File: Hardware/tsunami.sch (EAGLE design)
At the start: 154 parts, among them J1 CORTEX_DEBUGPTH, J10 3.3V, J100 AUDIO I/O, J101 USD-SDIO-SOCKET, J102 USB-MICROB", J12 !PLAYING, J3 FTDI_DEVICE, J5 AOUT5L, J6 AOUT5R, J7 AIN2L, J8 AIN2R, J9 3.3VA, Q1 2.5A/30V, U1 ATSAMS70NXXA-AN, U2 AK4618VQSFE-PACKAGE, U3 LM1117, U4 LM1117, U5 6N138M, U6 74AHC1G125, Y2 11.2896 MHz

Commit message: Somehow forgot schem with last commit.
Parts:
- removed J100: AUDIO I/O, SparkFun-Connectors:M10X2
- removed J101: USD-SDIO-SOCKET, SparkFun-Connectors:USD-SDIO-SOCKET
- removed J102: USB-MICROB", SparkFun-Connectors:USB-MICROB"
- removed J16, J17: (no value), SparkFun-Connectors:M02PTH
- added J13: GND, SparkFun-Connectors:M01PTH_NO_SILK_YES_STOP
- added TP1: AIN2L, SparkFun-Passives:TEST-POINTTP_15TH_THRU
- added TP2: AIN2R, SparkFun-Passives:TEST-POINTTP_15TH_THRU
- added TP3: AOUT5L, SparkFun-Passives:TEST-POINTTP_15TH_THRU
- added TP4: AOUT5R, SparkFun-Passives:TEST-POINTTP_15TH_THRU
- C1: value 12pF -> 10nF; device SparkFun-Capacitors:12PF-50V-5%(0603) -> SparkFun-Capacitors:10NF/10000PF-50V-10%(0603)
- C12: value 10uF -> 0.1uF; device SparkFun-Capacitors:10UF-6.3V-20%(0603) -> SparkFun-Capacitors:0.1UF-25V(+80/-20%)(0603)
- C13, C15, C17, C19, C21, C22, C23, C24, C26, C28, C31: value 1.0uF -> 0.1uF; device SparkFun-Capacitors:1.0UF-16V-10%(0603) -> SparkFun-Capacitors:0.1UF-25V(+80/-20%)(0603)
- C14: value 0.1uF -> 4.7uF; device SparkFun-Capacitors:0.1UF-25V(+80/-20%)(0603) -> SparkFun-Capacitors:4.7UF-6.3V-10%(0603)0603
- C2: value 12pF -> 10uF; device SparkFun-Capacitors:12PF-50V-5%(0603) -> SparkFun-Capacitors:10UF-6.3V-20%(0603)
- C20: value 1.0uF -> 10pF; device SparkFun-Capacitors:1.0UF-16V-10%(0603) -> SparkFun-Capacitors:10PF-50V-5%(0603)
- C25: value 1.0uF -> 2.2uF; device SparkFun-Capacitors:1.0UF-16V-10%(0603) -> SparkFun-Capacitors:2.2UF-10V-20%(0603)
- C27: value 1.0uF -> 10uF; device SparkFun-Capacitors:1.0UF-16V-10%(0603) -> SparkFun-Capacitors:10UF-6.3V-20%(0603)
- C29: value 4.7uF -> 1.0uF; device SparkFun-Capacitors:4.7UF-6.3V-10%(0603)0603 -> SparkFun-Capacitors:1.0UF-16V-10%(0603)
- C30: value 10nF -> 1.0uF; device SparkFun-Capacitors:10NF/10000PF-50V-10%(0603) -> SparkFun-Capacitors:1.0UF-16V-10%(0603)
- C33, C39, C40, C41, C42, C43, C44, C45, C46: value 0.1uF -> 1.0uF; device SparkFun-Capacitors:0.1UF-25V(+80/-20%)(0603) -> SparkFun-Capacitors:1.0UF-16V-10%(0603)
- C34: value 10pF -> 1.0uF; device SparkFun-Capacitors:10PF-50V-5%(0603) -> SparkFun-Capacitors:1.0UF-16V-10%(0603)
- C36: value 10uF -> 1.0uF; device SparkFun-Capacitors:10UF-6.3V-20%(0603) -> SparkFun-Capacitors:1.0UF-16V-10%(0603)
- C37: device SparkFun-Capacitors:0.1UF-25V-5%(0603) -> SparkFun-Capacitors:0.1UF-25V(+80/-20%)(0603)
- C38: value 0.1uF -> 1.0uF; device SparkFun-Capacitors:0.1UF-25V-5%(0603) -> SparkFun-Capacitors:1.0UF-16V-10%(0603)
- C47, C48: device SparkFun-Capacitors:0.1UF-25V(+80/-20%)(0603) -> SparkFun-Capacitors:0.1UF-25V-5%(0603)
- C5: value 0.1uF -> 10uF; device SparkFun-Capacitors:0.1UF-25V(+80/-20%)(0603) -> SparkFun-Capacitors:10UF-6.3V-20%(0603)
- C6: value 2.2uF -> 10uF; device SparkFun-Capacitors:2.2UF-10V-20%(0603) -> SparkFun-Capacitors:10UF-6.3V-20%(0603)
- C7, C9: value 10uF -> 12pF; device SparkFun-Capacitors:10UF-6.3V-20%(0603) -> SparkFun-Capacitors:12PF-50V-5%(0603)
- D1: value BLUE -> MBRA140; device SparkFun-LED:LED-BLUE0603 -> SparkFun-DiscreteSemi:DIODE-SCHOTTKY-MBRA140
- D2: value MBRA140 -> BLUE; device SparkFun-DiscreteSemi:DIODE-SCHOTTKY-MBRA140 -> SparkFun-LED:LED-BLUE0603
- J1: value CORTEX_DEBUGPTH -> VDC-IN; device SparkFun-Connectors:CORTEX_DEBUGPTH -> SparkFun-Connectors:M02PTH
- J10: value 3.3V -> TRIG2; device SparkFun-Connectors:M01PTH_NO_SILK_YES_STOP -> SparkFun-Connectors:M08X2
- J11: value (none) -> TRIG1; device SparkFun-Connectors:M05NO_SILK -> SparkFun-Connectors:M08X2
- J12: value !PLAYING -> USD-SDIO-SOCKET; device SparkFun-Connectors:M01PTH_NO_SILK_YES_STOP -> SparkFun-Connectors:USD-SDIO-SOCKET
- J14: value (none) -> AUDIO I/O; device SparkFun-Connectors:M08X2 -> SparkFun-Connectors:M10X2
- J15: value (none) -> MIDI; device SparkFun-Connectors:M01PTH_NO_SILK_YES_STOP -> SparkFun-Connectors:M05NO_SILK
- J2: value (none) -> GND-IN; device SparkFun-Connectors:M01PTH_NO_SILK_YES_STOP -> SparkFun-Connectors:M02PTH
- J3: value FTDI_DEVICE -> DEBUG; device SparkFun-Connectors:FTDI_DEVICE -> SparkFun-Connectors:M01PTH_NO_SILK_YES_STOP
- J4: value (none) -> USB-MICROB"; device SparkFun-Connectors:M08X2 -> SparkFun-Connectors:USB-MICROB"
- J5: value AOUT5L -> CORTEX_DEBUGPTH; device SparkFun-Passives:TEST-POINTTP_15TH_THRU -> SparkFun-Connectors:CORTEX_DEBUGPTH
- J6: value AOUT5R -> 3.3VA; device SparkFun-Passives:TEST-POINTTP_15TH_THRU -> SparkFun-Connectors:M01PTH_NO_SILK_YES_STOP
- J7: value AIN2L -> 3.3V; device SparkFun-Passives:TEST-POINTTP_15TH_THRU -> SparkFun-Connectors:M01PTH_NO_SILK_YES_STOP
- J8: value AIN2R -> !PLAYING; device SparkFun-Passives:TEST-POINTTP_15TH_THRU -> SparkFun-Connectors:M01PTH_NO_SILK_YES_STOP
- J9: value 3.3VA -> FTDI_DEVICE; device SparkFun-Connectors:M01PTH_NO_SILK_YES_STOP -> SparkFun-Connectors:FTDI_DEVICE
- L1: value 470 -> 10uH; device SparkFun-Passives:INDUCTOR0603 -> SparkFun-Passives:INDUCTOR0805; PROD_ID NDUC-12579 -> NDUC-13231
- L4: value 10uH -> 470; device SparkFun-Passives:INDUCTOR0805 -> SparkFun-Passives:INDUCTOR0603; PROD_ID NDUC-13231 -> NDUC-12579
- LOGO1: value SFE_LOGO_NAME_FLAME.2_INCH -> SFE_LOGO_NAME.2_INCH; device SparkFun-Aesthetics:SFE_LOGO_NAME_FLAME.2_INCH -> SparkFun-Aesthetics:SFE_LOGO_NAME.2_INCH
- LOGO3: value SFE_LOGO_NAME.2_INCH -> OSHW-LOGOM; device SparkFun-Aesthetics:SFE_LOGO_NAME.2_INCH -> SparkFun-Aesthetics:OSHW-LOGOM
- R1: value 100k -> 33; device SparkFun-Resistors:100KOHM-1/10W-1%(0603) -> SparkFun-Resistors:33OHM1/10W1%(0603)
- R11, R12: value 100k -> 240; device SparkFun-Resistors:100KOHM-1/10W-1%(0603) -> SparkFun-Resistors:240OHM1/10W1%(0603)
- R13: value 100k -> 330; device SparkFun-Resistors:100KOHM-1/10W-1%(0603) -> SparkFun-Resistors:330OHM1/10W1%(0603)
- R14: value 5.62k -> 4.7K; device SparkFun-Resistors:5.62KOHM1/10W1%(0603) -> SparkFun-Resistors:4.7KOHM-1/10W-1%(0603)
- R15: value 15K -> 4.7K; device SparkFun-Resistors:15KOHM1/10W1%(0603)0603 -> SparkFun-Resistors:4.7KOHM-1/10W-1%(0603)
- R16: value 22K -> 2.2; device SparkFun-Resistors:22KOHM1/10W1%(0603) -> SparkFun-Resistors:2.2OHM-1/10W-5%(0603)
- R17: value 2.2 -> 5.62k; device SparkFun-Resistors:2.2OHM-1/10W-5%(0603) -> SparkFun-Resistors:5.62KOHM1/10W1%(0603)
- R18: value 240 -> 10K; device SparkFun-Resistors:240OHM1/10W1%(0603) -> SparkFun-Resistors:10KOHM-1/10W-1%(0603)0603
- R19: value 240 -> 100k; device SparkFun-Resistors:240OHM1/10W1%(0603) -> SparkFun-Resistors:100KOHM-1/10W-1%(0603)
- R2: value 100k -> 1M; device SparkFun-Resistors:100KOHM-1/10W-1%(0603) -> SparkFun-Resistors:1MOHM-1/10W-1%(0603)
- R20, R21: value 390 -> 100k; device SparkFun-Resistors:390OHM1/10W1%(0603) -> SparkFun-Resistors:100KOHM-1/10W-1%(0603)
- R23, R3: value 100k -> 10K; device SparkFun-Resistors:100KOHM-1/10W-1%(0603) -> SparkFun-Resistors:10KOHM-1/10W-1%(0603)0603
- R24: value 100k -> 100; device SparkFun-Resistors:100KOHM-1/10W-1%(0603) -> SparkFun-Resistors:100OHM-1/10W-1%(0603)
- R25, R26: value 4.7K -> 100; device SparkFun-Resistors:4.7KOHM-1/10W-1%(0603) -> SparkFun-Resistors:100OHM-1/10W-1%(0603)
- R27: value 33 -> 100; device SparkFun-Resistors:33OHM1/10W1%(0603) -> SparkFun-Resistors:100OHM-1/10W-1%(0603)
- R28: value 10K -> 100; device SparkFun-Resistors:10KOHM-1/10W-1%(0603)0603 -> SparkFun-Resistors:100OHM-1/10W-1%(0603)
- R29: value 1M -> 100k; device SparkFun-Resistors:1MOHM-1/10W-1%(0603) -> SparkFun-Resistors:100KOHM-1/10W-1%(0603)
- R32, R33, R34, R35, R36: value 10 -> 100k; device SparkFun-Resistors:10OHM-1/10W-1%(0603)SMD -> SparkFun-Resistors:100KOHM-1/10W-1%(0603)
- R4: value 100k -> 15K; device SparkFun-Resistors:100KOHM-1/10W-1%(0603) -> SparkFun-Resistors:15KOHM1/10W1%(0603)0603
- R40, R41, R43, R44: value 100 -> 10; device SparkFun-Resistors:100OHM-1/10W-1%(0603) -> SparkFun-Resistors:10OHM-1/10W-1%(0603)SMD
- R42: value 220 -> 10; device SparkFun-Resistors:220OHM-1/10W-1%(0603) -> SparkFun-Resistors:10OHM-1/10W-1%(0603)SMD
- R45: value 100 -> 220; device SparkFun-Resistors:100OHM-1/10W-1%(0603) -> SparkFun-Resistors:220OHM-1/10W-1%(0603)
- R5: value 10K -> 22K; device SparkFun-Resistors:10KOHM-1/10W-1%(0603)0603 -> SparkFun-Resistors:22KOHM1/10W1%(0603)
- R6: value 10K -> 100k; device SparkFun-Resistors:10KOHM-1/10W-1%(0603)0603 -> SparkFun-Resistors:100KOHM-1/10W-1%(0603)
- R7: value 330 -> 390; device SparkFun-Resistors:330OHM1/10W1%(0603) -> SparkFun-Resistors:390OHM1/10W1%(0603)
- R8: value 100k -> 390; device SparkFun-Resistors:100KOHM-1/10W-1%(0603) -> SparkFun-Resistors:390OHM1/10W1%(0603)
- S3: value DNS -> User; device SparkFun-Electromechanical:SWITCH-MOMENTARY-2SIDE_EZ -> SparkFun-Electromechanical:SWITCH-MOMENTARY-2SMD
- S4: value User -> DNS; device SparkFun-Electromechanical:SWITCH-MOMENTARY-2SMD -> SparkFun-Electromechanical:SWITCH-MOMENTARY-2SIDE_EZ
- U1: value ATSAMS70NXXA-AN -> LM1117; device tapestry:ATSAMS70NXXA-AN -> SparkFun-PowerIC:V_REG_LM1117SOT223
- U2: value AK4618VQSFE-PACKAGE -> LM1117; device tapestry:AK4618VQSFE-PACKAGE -> SparkFun-PowerIC:V_REG_LM1117SOT223
- U3: value LM1117 -> ATSAMS70NXXA-AN; device SparkFun-PowerIC:V_REG_LM1117SOT223 -> tapestry:ATSAMS70NXXA-AN
- U4: value LM1117 -> AK4618VQSFE-PACKAGE; device SparkFun-PowerIC:V_REG_LM1117SOT223 -> tapestry:AK4618VQSFE-PACKAGE
- U5: value 6N138M -> 74AHC1G125; device SparkFun-DiscreteSemi:OPTO_DARL_6N138S -> SparkFun-DigitalIC:74AHC1G125
- U6: value 74AHC1G125 -> 6N138M; device SparkFun-DigitalIC:74AHC1G125 -> SparkFun-DiscreteSemi:OPTO_DARL_6N138S
- renumbered STANDOFF1 to H3, STANDOFF2 to H1, STANDOFF3 to H2, STANDOFF4 to H4, Y2 to Y1
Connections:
- removed net VCC: R46.2, R47.2, U5.VCC, U6.VCC
- net 3.3V: now also C10.1, C15.1, C27.1, C28.1, C35.1, C36.1, C6.1, C8.1, J12.VCC, J5.VCC, J7.1, L4.1, R10.2, R12.2, R13.2, R14.2, R15.2, R16.1, R18.2, R20.2, R21.2, R47.2, R48.2, R9.2, U2.OUT, U2.OUT@1, U3.VDDIN, U3.VDDIO@1, U3.VDDIO@2, U3.VDDIO@3, U3.VDDIO@4, U3.VDDUTMII, U4.TVDD, U5.VCC, U6.VCC; no longer C33.1, C43.1, C44.1, C45.1, C46.1, C47.1, C48.1, C7.1, J1.VCC, J10.1, J101.VCC, L3.1, R1.2, R17.1, R2.2, R24.2, R25.2, R26.2, R28.2, R4.2, R5.2, R7.2, U1.VDDIN, U1.VDDIO@1, U1.VDDIO@2, U1.VDDIO@3, U1.VDDIO@4, U1.VDDUTMII, U2.TVDD, U4.OUT, U4.OUT@1
- net 3.3V_A: now also C31.1, C32.1, C37.1, C38.1, C5.1, J6.1, R11.2, U1.OUT, U1.OUT@1, U4.AVDD1, U4.AVDD2; no longer C14.1, C17.1, C18.1, C19.1, C9.1, J9.1, R18.2, U2.AVDD1, U2.AVDD2, U3.OUT, U3.OUT@1
- net 56: now also R45.2, U6.A; no longer R42.2, U5.A
- net AIN1L: now also C29.1, J14.17; no longer C25.1, J100.17
- net AIN1R: now also C30.1, J14.19; no longer C26.1, J100.19
- net AIN2L: now also TP1.1, U4.IN3N; no longer J7.1, U2.IN3N
- net AIN2R: now also TP2.1, U4.IN4N; no longer J8.1, U2.IN4N
- net AOUT1L: now also C47.1, J14.1, R37.2; no longer C37.1, J100.1, R32.2
- net AOUT1R: now also C48.1, J14.3, R38.2; no longer C38.1, J100.3, R33.2
- net AOUT2L: now also J14.5, R39.2; no longer J100.5, R34.2
- net AOUT2R: now also J14.7, R40.2; no longer J100.7, R35.2
- net AOUT3L: now also J14.9, R41.2; no longer J100.9, R36.2
- net AOUT3R: now also J14.11, R42.2; no longer J100.11, R37.2
- net AOUT4L: now also J14.13, R43.2; no longer J100.13, R38.2
- net AOUT4R: now also J14.15, R44.2; no longer J100.15, R39.2
- net APDN: now also U3.PA01, U4.PDN; no longer U1.PA01, U2.PDN
- net BCLK: now also R26.1, U3.PB01; no longer R44.1, U1.PB01
- net BCLK_C: now also R26.2, U4.BICK; no longer R44.2, U2.BICK
- net DBUG: now also J3.1, U3.PA00; no longer J2.1, U1.PA00
- net GND: now also C21.2, C22.2, C23.2, C24.2, C25.2, C26.2, C27.2, C28.2, C31.2, C32.2, J10.10, J10.12, J10.14, J10.16, J10.2, J10.4, J10.6, J10.8, J11.10, J11.12, J11.14, J11.16, J11.2, J11.4, J11.6, J11.8, J12.GND, J12.SHIELD@1, J12.SHIELD@3, J13.1, J14.18, J14.20, J15.5, J2.1, J2.2, J4.GND, J5.GND@3, J5.GND@5, J5.GNDDTCT, J9.GND, R17.1, R2.1, R32.1, R33.1, R34.1, R35.1, R36.1, R5.1, R7.1, U3.GND@1, U3.GND@2, U3.GND@3, U3.GND@4, U3.GND@5, U3.GND@6, U3.VREFN, U4.STDI2, U4.STDI3, U4.STDI4, U4.STDI5, U4.STDI6/TDMI, U4.VSS1, U4.VSS2, U4.VSS3, U5./OE; no longer C29.2, C30.2, C39.2, C40.2, C41.2, C42.2, C43.2, C44.2, C45.2, C46.2, J1.GND@3, J1.GND@5, J1.GNDDTCT, J100.10, J100.12, J100.14, J100.16, J100.18, J100.2, J100.20, J100.4, J100.6, J100.8, J101.GND, J101.SHIELD@1, J101.SHIELD@3, J102.GND, J11.5, J15.1, J17.1, J17.2, J3.GND, J4.10, J4.12, J4.14, J4.16, J4.2, J4.4, J4.6, J4.8, R10.1, R11.1, R12.1, R13.1, R14.1, R16.1, R20.1, R21.1, R9.1, U1.GND@1, U1.GND@2, U1.GND@3, U1.GND@4, U1.GND@5, U1.GND@6, U1.VREFN, U2.STDI2, U2.STDI3, U2.STDI4, U2.STDI5, U2.STDI6/TDMI, U2.VSS1, U2.VSS2, U2.VSS3, U6./OE
- net HSDM: now also J4.D-, U3.HSDM; no longer J102.D-, U1.HSDM
- net HSDP: now also J4.D+, U3.HSDP; no longer J102.D+, U1.HSDP
- net I2C_SCK: now also R15.1, U3.PA04, U4.SCL; no longer R26.1, U1.PA04, U2.SCL
- net I2C_SDA: now also R14.1, U3.PA03, U4.SDA; no longer R25.1, U1.PA03, U2.SDA
- net LRCK: now also R27.1, U3.PB00; no longer R45.1, U1.PB00
- net LRCK_C: now also R27.2, U4.LRCLK; no longer R45.2, U2.LRCLK
- net MCLK: now also R25.1, U3.PA18; no longer R43.1, U1.PA18
- net MCLK_C: now also R25.2, U4.MCLK; no longer R43.2, U2.MCLK
- net MIDI-IN-PIN4: now also J15.1, R45.1; no longer J11.1, R42.1
- net MIDI-IN-PIN5: now also J15.2, U6.C; no longer J11.2, U5.C
- net MIDI-OUT-PIN4: now also J15.3; no longer J11.3
- net MIDI-OUT-PIN5: now also J15.4, R46.2; no longer J11.4, R48.2
- net MIN: now also R48.1, U3.PD15, U6.VOUT; no longer R46.1, U1.PD15, U5.VOUT
- net MOUT: now also U3.PD16, U5.A; no longer U1.PD16, U6.A
- net N$1: now also C7.1, U3.PB08; no longer C2.1, U1.PB08
- net N$10: now also D2.C, U3.PA23; no longer D1.C, U1.PA23
- net N$11: now also D2.A, R13.1; no longer D1.A, R7.1
- net N$12: now also C34.1, U4.VCOM; no longer C20.1, U2.VCOM
- net N$13: now also C40.1, U4.LOUT1; no longer C21.1, U2.LOUT1
- net N$14: now also C30.2, U4.IN2/IN2P; no longer C26.2, U2.IN2/IN2P
- net N$15: now also C29.2, U4.IN1/IN1P; no longer C25.2, U2.IN1/IN1P
- net N$16: now also C20.1, R17.2, U3.VBG; no longer C34.1, R14.2, U1.VBG
- net N$17: now also C26.1, L4.2, U3.VREFP; no longer C35.1, L3.2, U1.VREFP
- net N$18: now also C43.1, U4.ROUT1; no longer C22.1, U2.ROUT1
- net N$19: now also C45.1, U4.LOUT2; no longer C23.1, U2.LOUT2
- net N$2: now also C9.1, U3.PB09; no longer C1.1, U1.PB09
- net N$20: now also C41.1, U4.ROUT2; no longer C24.1, U2.ROUT2
- net N$21: now also C44.1, U4.LOUT3; no longer C27.1, U2.LOUT3
- net N$22: now also C46.1, U4.ROUT3; no longer C28.1, U2.ROUT3
- net N$23: now also C40.2, R31.2, R37.1; no longer C21.2, R32.1, R8.2
- net N$24: now also L1.1, R16.2; no longer L4.1, R17.2
- net N$25: now also R11.1, R7.2, U1.ADJ; no longer R18.1, R20.2, U3.ADJ
- net N$26: now also R1.1; no longer R27.1
- net N$27: now also C42.2, R44.1; no longer C32.2, R39.1
- net N$28: now also C39.2, R29.2, R43.1; no longer C31.2, R31.2, R38.1
- net N$29: now also R12.1, R8.2, U2.ADJ; no longer R19.1, R21.2, U4.ADJ
- net N$3: now also C19.1, L2.1, U3.VDDUTMIC; no longer C3.1, L1.1, U1.VDDUTMIC
- net N$30: now also C46.2, R36.2, R42.1; no longer C28.2, R13.2, R37.1
- net N$31: now also C39.1, U4.LOUT4; no longer C31.1, U2.LOUT4
- net N$32: now also C42.1, U4.ROUT4; no longer C32.1, U2.ROUT4
- net N$33: now also TP3.1, U4.LOUT5; no longer J5.1, U2.LOUT5
- net N$34: now also TP4.1, U4.ROUT5; no longer J6.1, U2.ROUT5
- net N$38: now also R46.1, U5.Y; no longer R48.1, U6.Y
- net N$4: now also C14.1, L1.2, U3.VDDPLLUSB; no longer C29.1, L4.2, U1.VDDPLLUSB
- net N$5: now also C23.1, L3.1, U3.VDDPLL; no longer C4.1, L2.1, U1.VDDPLL
- net N$52: now also C44.2, R35.2, R41.1; no longer C27.2, R12.2, R36.1
- net N$53: now also C41.2, R34.2, R40.1; no longer C24.2, R11.2, R35.1
- net N$54: now also C43.2, R32.2, R38.1; no longer C22.2, R33.1, R9.2
- net N$55: now also C45.2, R33.2, R39.1; no longer C23.2, R10.2, R34.1
- net N$6: now also C33.1, U4.REGO; no longer C15.1, U2.REGO
- net N$7: now also C2.1, D1.A, J4.VBUS, R4.2; no longer C36.1, D2.A, J102.VBUS, R15.2
- net N$75: now also R2.2; no longer R29.2
- net N$8: now also J8.1, U3.PA16; no longer J12.1, U1.PA16
- net NRESET: now also C1.1, J5.NRESET, R1.2, R10.1, R3.1, U3.NRST; no longer C30.1, J1.NRESET, R24.1, R27.2, R28.1, U1.NRST
- net REGINPUTS: now also C3.1, C4.1, D1.C, U1.IN, U2.IN; no longer C10.1, C8.1, D2.C, U3.IN, U4.IN
- net RXD: now also J9.RXI, U3.PD28; no longer J3.RXI, U1.PD28
- net SDCD: now also J12.CD1, J12.CD2, R18.1, U3.PD18; no longer J101.CD1, J101.CD2, R6.1, U1.PD18
- net SDCLK: now also J12.CLK, U3.PA25; no longer J101.CLK, U1.PA25
- net SDCMD: now also J12.CMD, R23.1, U3.PA28; no longer J101.CMD, R5.1, U1.PA28
- net SDD0: now also J12.DAT0, R21.1, U3.PA30; no longer J101.DAT0, R3.1, U1.PA30
- net SDD1: now also J12.DAT1, R22.1, U3.PA31; no longer J101.DAT1, R4.1, U1.PA31
- net SDD2: now also J12.DAT2, R19.1, U3.PA26; no longer J101.DAT2, R1.1, U1.PA26
- net SDD3: now also J12.CD/DAT3, R20.1, U3.PA27; no longer J101.CD/DAT3, R2.1, U1.PA27
- net SWCLK/TCK: now also J5.SWDCLK/TCK, R9.1, U3.PB07; no longer J1.SWDCLK/TCK, R23.1, U1.PB07
- net SWDIO/TMS: now also J5.SWDIO/TMS, R6.1, U3.PB06; no longer J1.SWDIO/TMS, R22.1, U1.PB06
- net TDI: now also J5.NC/TDI, U3.PB04; no longer J1.NC/TDI, U1.PB04
- net TDMI: now also R24.1, U3.PA10; no longer R40.1, U1.PA10
- net TDMI_C: now also R24.2, U4.STDO1; no longer R40.2, U2.STDO1
- net TDMO: now also R28.1, U3.PD26; no longer R41.1, U1.PD26
- net TDMO_C: now also R28.2, U4.STDI1; no longer R41.2, U2.STDI1
- net TDO: now also J5.SWO/TDO, U3.PB05; no longer J1.SWO/TDO, U1.PB05
- net TXD: now also J9.TXO, U3.PD30; no longer J3.TXO, U1.PD30
- net UIA1: now also J10.7, U3.PB02; no longer J4.7, U1.PB02
- net UIA2: now also J10.5, U3.PB03; no longer J4.5, U1.PB03
- net UIA3: now also J10.3, U3.PA21; no longer J4.3, U1.PA21
- net UIA4: now also J10.1, U3.PA17; no longer J4.1, U1.PA17
- net UID1: now also J11.15, U3.PD12; no longer J14.15, U1.PD12
- net UID10: now also J10.13, U3.PD02; no longer J4.13, U1.PD02
- net UID11: now also J10.11, U3.PD01; no longer J4.11, U1.PD01
- net UID12: now also J10.9, U3.PD00; no longer J4.9, U1.PD00
- net UID2: now also J11.13, U3.PD11; no longer J14.13, U1.PD11
- net UID3: now also J11.11, U3.PD09; no longer J14.11, U1.PD09
- net UID4: now also J11.9, U3.PD08; no longer J14.9, U1.PD08
- net UID5: now also J11.7, U3.PD07; no longer J14.7, U1.PD07
- net UID6: now also J11.5, U3.PD06; no longer J14.5, U1.PD06
- net UID7: now also J11.3, U3.PD05; no longer J14.3, U1.PD05
- net UID8: now also J11.1, U3.PD04; no longer J14.1, U1.PD04
- net UID9: now also J10.15, U3.PD03; no longer J4.15, U1.PD03
- net USERSW: now also U3.PA22; no longer U1.PA22
- net VBDET: now also R4.1, R5.2, U3.PD19; no longer R15.1, R16.2, U1.PD19
- net VDDOUT: now also C17.1, C18.1, C21.1, C22.1, C24.1, C25.1, L3.2, U3.VDDCORE@1, U3.VDDCORE@2, U3.VDDCORE@3, U3.VDDCORE@4, U3.VDDOUT; no longer C39.1, C40.1, C41.1, C42.1, C5.1, C6.1, L1.2, U1.VDDCORE@1, U1.VDDCORE@2, U1.VDDCORE@3, U1.VDDCORE@4, U1.VDDOUT
- net VIN: now also J1.1, J1.2; no longer J16.1, J16.2
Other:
- note added: "Codec is at I2C address 0x20"
- note added: "Isolated analog ground plane with single connection to digital ground. JP1, JP2, JP3 are being used to formalize the plane crossing."
- note added: "J8 is active low "playing" indicator."
- note removed: "Isolated analog ground plane with single connection to digital ground"
- note removed: "J12 is active low "playing" indicator."
- moved on the sheet: C1, C10, C11, C12, C2, C3, C31, C32, C37, C38, C4, C5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

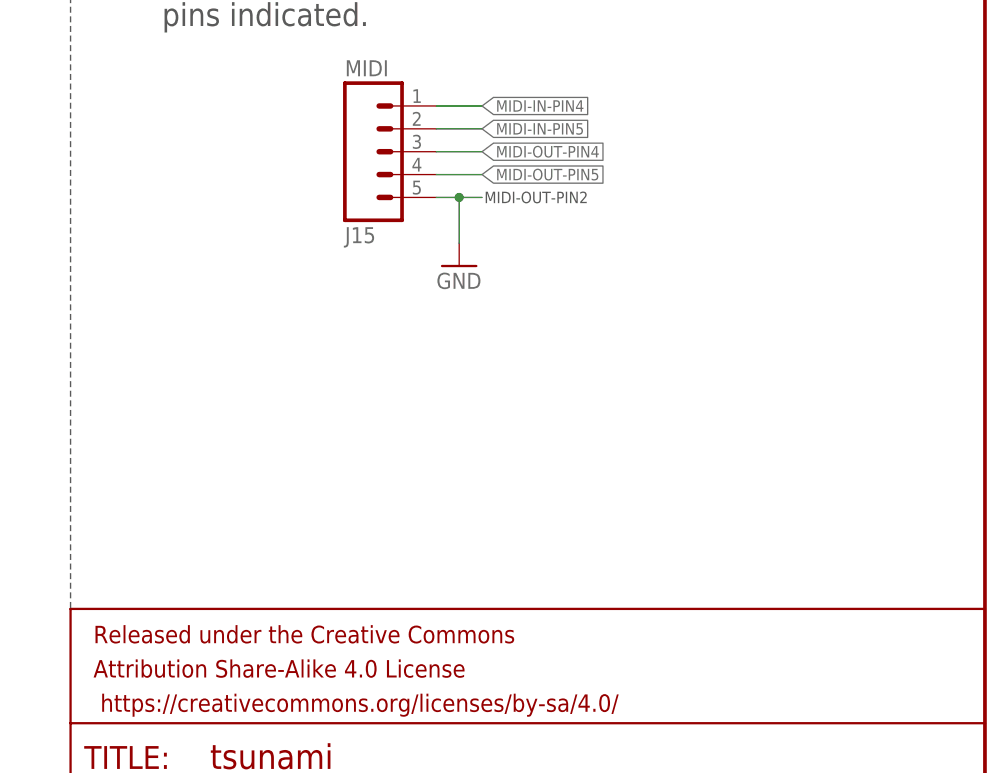
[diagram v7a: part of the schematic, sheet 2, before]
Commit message: Re-ordering MIDI output pins...
...so that they match the pin ordering on a DIN-5.
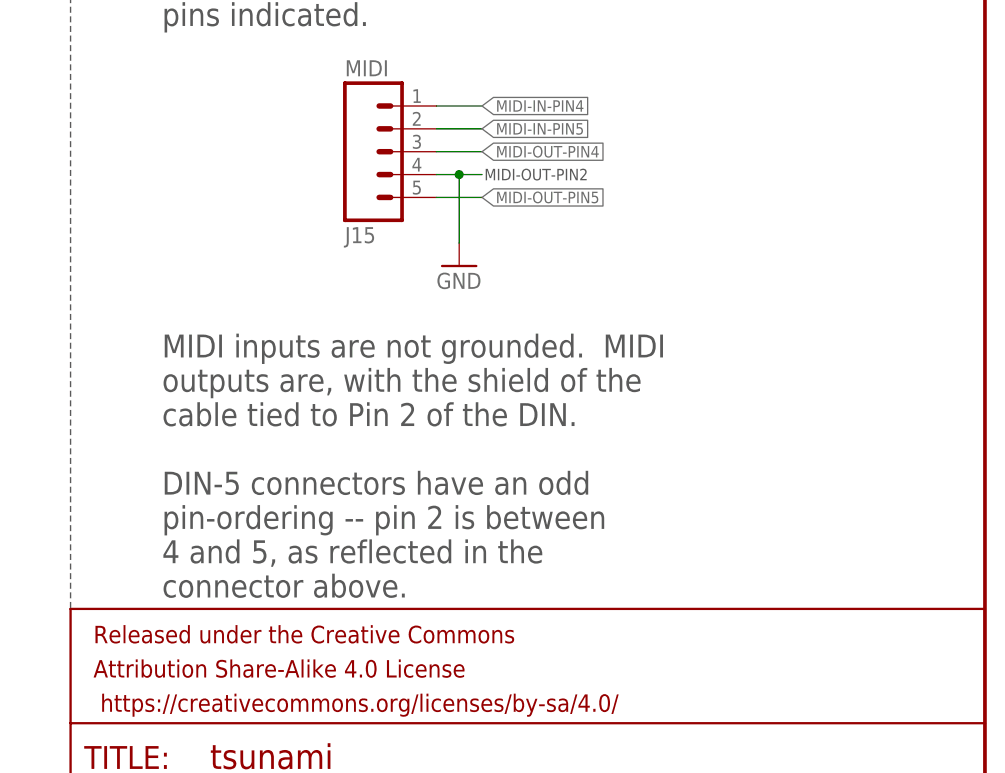
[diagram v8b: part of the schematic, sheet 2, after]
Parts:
- JP1, JP2, JP3: value JUMPER-PAD-2-NC_BY_TRACE -> JUMPER-PAD-2-NC_BY_TRACENO_SILK; device SparkFun-Passives:JUMPER-PAD-2-NC_BY_TRACE -> SparkFun-Passives:JUMPER-PAD-2-NC_BY_TRACENO_SILK
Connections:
- net GND: now also J15.4; no longer J15.5
- net MIDI-OUT-PIN5: now also J15.5; no longer J15.4
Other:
- note added: "MIDI inputs are not grounded. MIDI outputs are, with the shield of the cable tied to Pin 2 of the DIN. DIN-5 connectors have an odd pin-ordering -- pin 2 is between 4 and 5, as reflected in the connector above."
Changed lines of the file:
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@@
 <part name="GND47" library="SparkFun-Aesthetics" deviceset="GND" device=""/>
 <part name="GND49" library="SparkFun-Aesthetics" deviceset="GND" device=""/>
-<part name="JP3" library="SparkFun-Passives" deviceset="JUMPER-PAD-2-NC_BY_TRACE" device=""/>
-<part name="JP1" library="SparkFun-Passives" deviceset="JUMPER-PAD-2-NC_BY_TRACE" device=""/>
+<part name="JP3" library="SparkFun-Passives" deviceset="JUMPER-PAD-2-NC_BY_TRACE" device="NO_SILK" value="JUMPER-PAD-2-NC_BY_TRACENO_SILK"/>
+<part name="JP1" library="SparkFun-Passives" deviceset="JUMPER-PAD-2-NC_BY_TRACE" device="NO_SILK" value="JUMPER-PAD-2-NC_BY_TRACENO_SILK"/>
 <part name="GND41" library="SparkFun-Aesthetics" deviceset="GND" device=""/>
 <part name="GND42" library="SparkFun-Aesthetics" deviceset="GND" device=""/>
@@
 <part name="TP3" library="SparkFun-Passives" deviceset="TEST-POINT" device="TP_15TH_THRU" value="AOUT5L"/>
 <part name="TP4" library="SparkFun-Passives" deviceset="TEST-POINT" device="TP_15TH_THRU" value="AOUT5R"/>
-<part name="JP2" library="SparkFun-Passives" deviceset="JUMPER-PAD-2-NC_BY_TRACE" device=""/>
+<part name="JP2" library="SparkFun-Passives" deviceset="JUMPER-PAD-2-NC_BY_TRACE" device="NO_SILK" value="JUMPER-PAD-2-NC_BY_TRACENO_SILK"/>
 <part name="GND46" library="SparkFun-Aesthetics" deviceset="GND" device=""/>
 <part name="C39" library="SparkFun-Capacitors" deviceset="1.0UF-16V-10%(0603)" device="" value="1.0uF"/>
@@
 connected.  Connect the pads below to the
 pins indicated.</text>
-<text x="376.174" y="81.28" size="1.27" layer="97" align="center-left">MIDI-OUT-PIN2</text>
+<text x="376.174" y="83.82" size="1.27" layer="97" align="center-left">MIDI-OUT-PIN2</text>
 <text x="2.54" y="195.58" size="1.778" layer="97">Codec is at I2C
 address 0x20</text>
+<text x="340.36" y="66.04" size="2.54" layer="97" font="vector" align="top-left">MIDI inputs are not grounded.  MIDI
+outputs are, with the shield of the
+cable tied to Pin 2 of the DIN.
+DIN-5 connectors have an odd
+pin-ordering -- pin 2 is between
+4 and 5, as reflected in the
+connector above.  </text>
 </plain>
 <instances>
@@
 </segment>
 <segment>
-<pinref part="J15" gate="G$1" pin="5"/>
-<wire x1="370.84" y1="81.28" x2="373.38" y2="81.28" width="0.1524" layer="91"/>
 <pinref part="GND51" gate="1" pin="GND"/>
-<wire x1="373.38" y1="76.2" x2="373.38" y2="81.28" width="0.1524" layer="91"/>
-<wire x1="373.38" y1="81.28" x2="375.92" y2="81.28" width="0.1524" layer="91"/>
-<junction x="373.38" y="81.28"/>
+<wire x1="373.38" y1="76.2" x2="373.38" y2="83.82" width="0.1524" layer="91"/>
+<wire x1="373.38" y1="83.82" x2="375.92" y2="83.82" width="0.1524" layer="91"/>
+<pinref part="J15" gate="G$1" pin="4"/>
+<wire x1="370.84" y1="83.82" x2="373.38" y2="83.82" width="0.1524" layer="91"/>
+<junction x="373.38" y="83.82"/>
 </segment>
 </net>
@@
 <net name="MIDI-OUT-PIN5" class="0">
 <segment>
-<pinref part="J15" gate="G$1" pin="4"/>
-<wire x1="370.84" y1="83.82" x2="375.92" y2="83.82" width="0.1524" layer="91"/>
-<label x="375.92" y="83.82" size="1.27" layer="95" xref="yes"/>
-</segment>
-<segment>
+<wire x1="370.84" y1="81.28" x2="375.92" y2="81.28" width="0.1524" layer="91"/>
+<label x="375.92" y="81.28" size="1.27" layer="95" xref="yes"/>
+<pinref part="J15" gate="G$1" pin="5"/>
+</segment>
+<segment>
